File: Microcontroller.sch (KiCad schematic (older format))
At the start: 14 parts, among them SW1 SW_Push, SW2 SW_Push, U2 PIC16F1939-IPT, Y1 Crystal

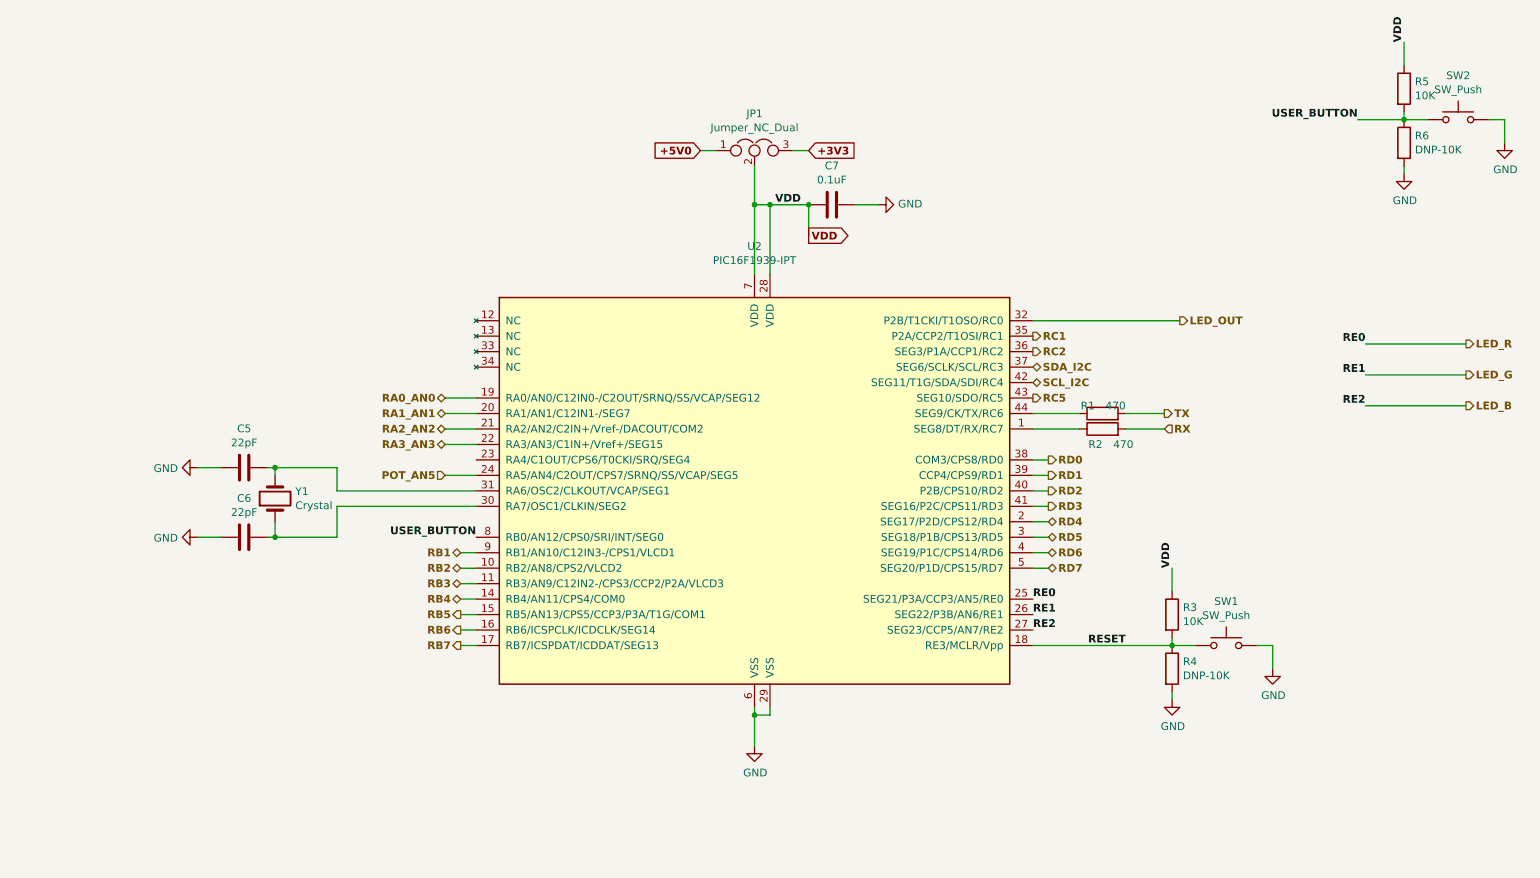
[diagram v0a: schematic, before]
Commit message: Se agrega bus a jerarquia y pines de programación icsp
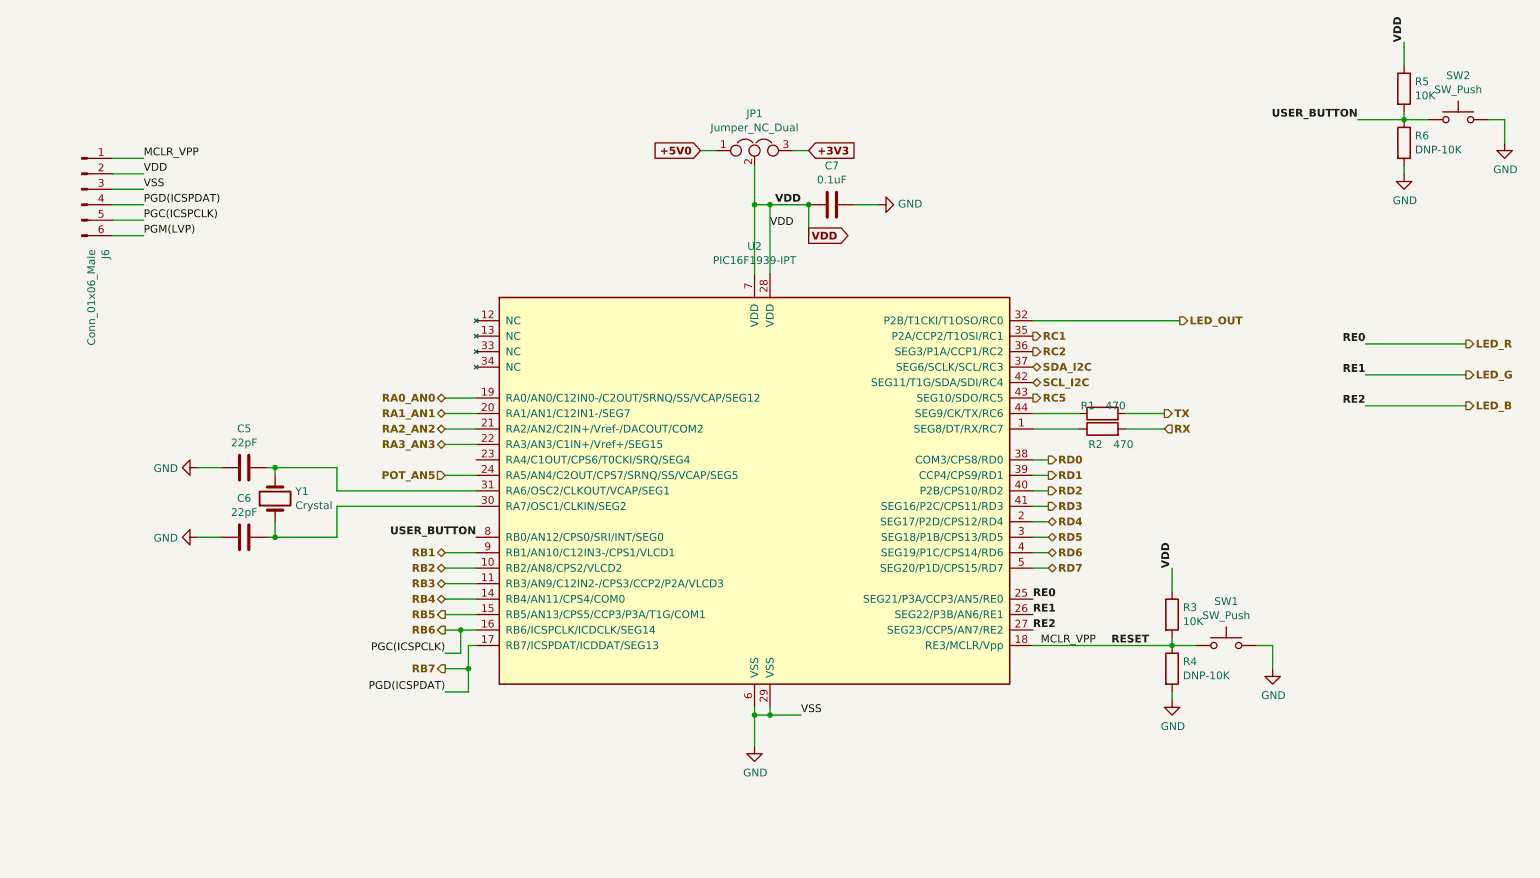
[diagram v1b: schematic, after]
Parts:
- added J6: Conn_01x06_Male, symbol Connector:Conn_01x06_Male
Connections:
- net GND: now also J6.3 (Pin_3)
- net RB6: now also J6.5 (Pin_5)
- net RB7: now also J6.4 (Pin_4)
- net VDD: now also J6.2 (Pin_2)
- net RESET renamed MCLR_VPP
- net MCLR_VPP: now also J6.1 (Pin_1)
- new net PGM(LVP): J6.6 (Pin_6)
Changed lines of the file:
@@
 EESchema Schematic File Version 4
+LIBS:TPDSI_1-cache
 EELAYER 29 0
 EELAYER END
@@
 Sheet 2 5
 Title "Kit Development for MCU PIC"
-Date "2019-05-05"
-Rev "1.0"
+Date "2019-05-06"
+Rev "1.1"
 Comp "Julian Bustamante Narvaez"
 Comment1 ""
@@
 	1    0    0    -1
 $EndComp
-Wire Wire Line
-	5850 5250 5850 5300
-Wire Wire Line
-	5950 5300 5950 5250
-Wire Wire Line
-	5850 5300 5950 5300
-Wire Wire Line
-	5850 5500 5850 5300
-Connection ~ 5850 5300
 $Comp
 L power:GND #PWR010
@@
 Text Label 4050 4150 2    50   ~ 10
 USER_BUTTON
-Text Label 8250 4850 2    50   ~ 10
+Text Label 8400 4850 2    50   ~ 10
 RESET
 Wire Wire Line
@@
 	1    0    0    -1
 $EndComp
-Wire Wire Line
-	4050 4850 3950 4850
-Text HLabel 3950 4850 0    50   Output ~ 10
+Text HLabel 3850 5000 0    50   Output ~ 10
 RB7
-Wire Wire Line
-	4050 4750 3950 4750
-Text HLabel 3950 4750 0    50   Output ~ 10
+Text HLabel 3850 4750 0    50   Output ~ 10
 RB6
-Wire Wire Line
-	4050 4650 3950 4650
-Text HLabel 3950 4650 0    50   Output ~ 10
+Text HLabel 3850 4650 0    50   Output ~ 10
 RB5
-Wire Wire Line
-	4050 4550 3950 4550
-Text HLabel 3950 4550 0    50   BiDi ~ 10
+Text HLabel 3850 4550 0    50   BiDi ~ 10
 RB4
-Wire Wire Line
-	4050 4450 3950 4450
-Text HLabel 3950 4450 0    50   BiDi ~ 10
+Text HLabel 3850 4450 0    50   BiDi ~ 10
 RB3
-Wire Wire Line
-	4050 4350 3950 4350
-Text HLabel 3950 4350 0    50   BiDi ~ 10
+Text HLabel 3850 4350 0    50   BiDi ~ 10
 RB2
-Wire Wire Line
-	4050 4250 3950 4250
-Text HLabel 3950 4250 0    50   BiDi ~ 10
+Text HLabel 3850 4250 0    50   BiDi ~ 10
 RB1
 Text HLabel 7650 2850 2    50   Output ~ 10
@@
 	6200 2200 6200 2000
 Connection ~ 6200 2000
+$Comp
+L Connector:Conn_01x06_Male J6
+U 1 1 5CD0F49A
+P 1500 1900
+F 0 "J6" V 1654 1512 50  0000 R CNN
+F 1 "Conn_01x06_Male" V 1563 1512 50  0000 R CNN
+F 2 "" H 1500 1900 50  0001 C CNN
+F 3 "~" H 1500 1900 50  0001 C CNN
+	1    1500 1900
+	1    0    0    -1
+$EndComp
+Wire Wire Line
+	1700 1700 1900 1700
+Wire Wire Line
+	1700 1800 1900 1800
+Wire Wire Line
+	1700 1900 1900 1900
+Wire Wire Line
+	1700 2000 1900 2000
+Wire Wire Line
+	1900 2100 1700 2100
+Wire Wire Line
+	1700 2200 1900 2200
+Text Label 1900 2200 0    50   ~ 0
+PGM(LVP)
+Text Label 1900 2100 0    50   ~ 0
+PGC(ICSPCLK)
+Text Label 1900 2000 0    50   ~ 0
+PGD(ICSPDAT)
+Text Label 1900 1900 0    50   ~ 0
+VSS
+Text Label 1900 1800 0    50   ~ 0
+VDD
+Text Label 1900 1700 0    50   ~ 0
+MCLR_VPP
+Text Label 3850 5150 2    50   ~ 0
+PGD(ICSPDAT)
+Text Label 7700 4850 0    50   ~ 0
+MCLR_VPP
+Text Label 5950 2150 0    50   ~ 0
+VDD
+Text Label 6150 5300 0    50   ~ 0
+VSS
+Wire Wire Line
+	5850 5250 5850 5300
+Wire Wire Line
+	6150 5300 5950 5300
+Wire Wire Line
+	5950 5300 5950 5250
+Wire Wire Line
+	5950 5300 5850 5300
+Connection ~ 5950 5300
+Connection ~ 5850 5300
+Wire Wire Line
+	5850 5300 5850 5500
+Text Label 3850 4900 2    50   ~ 0
+PGC(ICSPCLK)
+Wire Wire Line
+	4000 4850 4000 5000
+Wire Wire Line
+	3850 5000 4000 5000
+Connection ~ 4000 5000
+Wire Wire Line
+	3850 5150 4000 5150
+Wire Wire Line
+	4000 5000 4000 5150
+Wire Wire Line
+	3850 4750 3950 4750
+Wire Wire Line
+	4000 4850 4050 4850
+Connection ~ 3950 4750
+Wire Wire Line
+	3950 4750 4050 4750
+Wire Wire Line
+	3850 4250 4050 4250
+Wire Wire Line
+	3850 4350 4050 4350
+Wire Wire Line
+	3850 4450 4050 4450
+Wire Wire Line
+	3850 4550 4050 4550
+Wire Wire Line
+	3850 4650 4050 4650
+Wire Wire Line
+	3950 4900 3850 4900
+Wire Wire Line
+	3950 4750 3950 4900
 $EndSCHEMATC

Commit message: Se Organiza conexiones de alimentacion con elementos de la biblioteca power, se quitan algunas etiquetas y se coloca la fuente en hoja principal
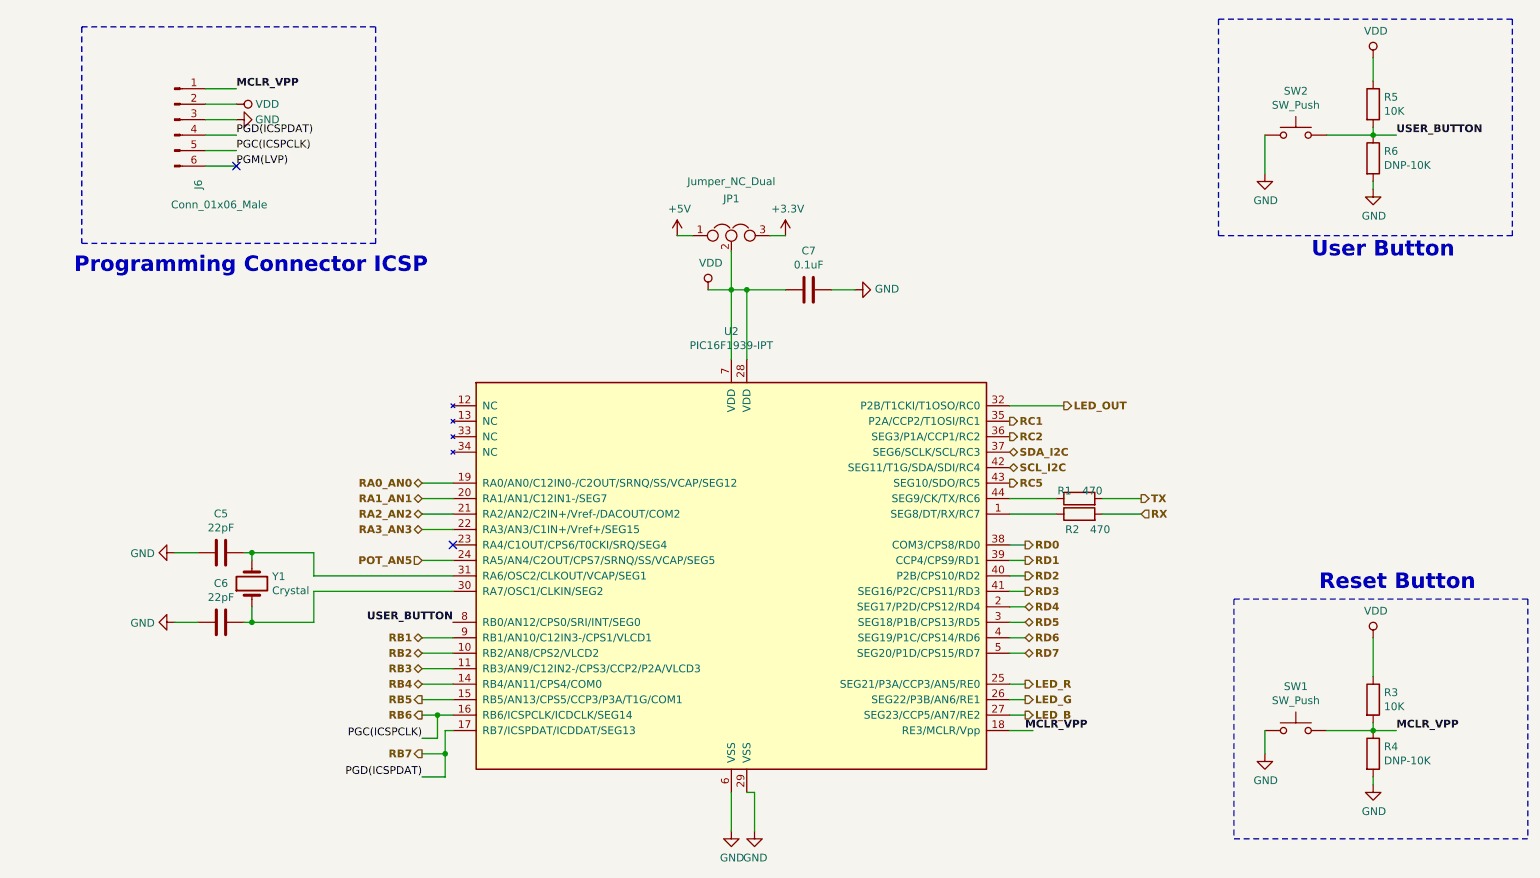
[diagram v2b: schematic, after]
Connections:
- net GND: now also SW1.1, SW2.1; no longer SW1.2, SW2.2
- net MCLR_VPP: now also SW1.2; no longer SW1.1
- net USER_BUTTON: now also SW2.2; no longer SW2.1
- net +5V0 renamed +5V
- no-connect marks 0 -> 2
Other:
- note added: "Programming Connector ICSP"
- note added: "Reset Button"
- note added: "User Button"
- moved on the sheet: C5, C6, C7, J6, JP1, R1, R2, R3, R4, R5, R6, SW1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

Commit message: Se agregan recomendaciones izq->dcha (In/Out), se Reorganiza jerarquía y bus de datos, se coloca graphics lines para indicar submodulos
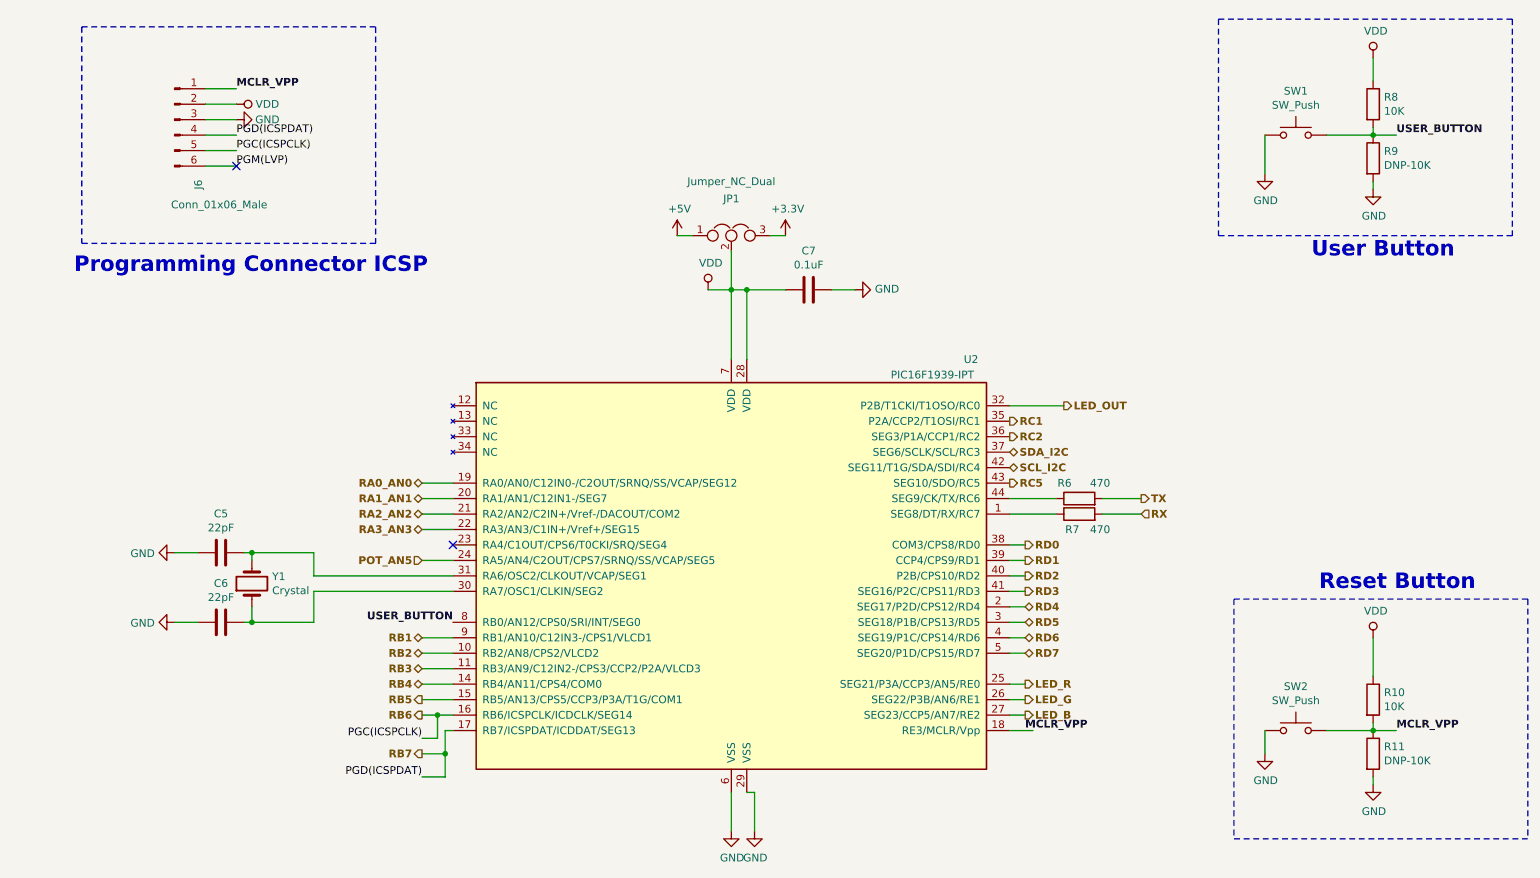
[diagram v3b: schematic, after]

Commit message: Se agrega ubicación de componentes, asociación de footprint, pendiente Ruteo.
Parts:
- C5, C6: footprint (none) -> Capacitor_SMD:C_0603_1608Metric; Part Number (none) -> 732-7748-1-ND
- C7: footprint (none) -> Capacitor_SMD:C_0603_1608Metric; Part Number (none) -> 732-7939-1-ND
- J6: footprint (none) -> Connector_PinSocket_2.54mm:PinSocket_1x06_P2.54mm_Vertical
- JP1: footprint (none) -> Connector_PinSocket_2.54mm:PinSocket_1x03_P2.54mm_Vertical
- R1, R2, R3, R4, R5, R6: footprint (none) -> Resistor_SMD:R_0603_1608Metric_Pad1.05x0.95mm_HandSolder
- SW1, SW2: footprint (none) -> Button_Switch_THT:SW_PUSH_6mm_H5mm; Part Number (none) -> 450-1804-ND
- U2: footprint (none) -> Package_QFP:TQFP-44_10x10mm_P0.8mm
- Y1: footprint (none) -> Crystal:Crystal_HC18-U_Vertical
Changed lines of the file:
@@
 F 0 "JP1" H 5700 2439 50  0000 C CNN
 F 1 "Jumper_NC_Dual" H 5700 2550 50  0000 C CNN
-F 2 "" H 5700 2200 50  0001 C CNN
+F 2 "Connector_PinSocket_2.54mm:PinSocket_1x03_P2.54mm_Vertical" H 5700 2200 50  0001 C CNN
 F 3 "~" H 5700 2200 50  0001 C CNN
 	1    5700 2200
@@
 F 0 "Y1" V 2646 4319 50  0000 R CNN
 F 1 "Crystal" V 2555 4319 50  0000 R CNN
-F 2 "" H 2600 4450 50  0001 C CNN
+F 2 "Crystal:Crystal_HC18-U_Vertical" H 2600 4450 50  0001 C CNN
 F 3 "~" H 2600 4450 50  0001 C CNN
 	1    2600 4450
@@
 F 0 "C5" V 2652 4250 50  0000 C CNN
 F 1 "22pF" V 2561 4250 50  0000 C CNN
-F 2 "" H 2438 4100 50  0001 C CNN
+F 2 "Capacitor_SMD:C_0603_1608Metric" H 2438 4100 50  0001 C CNN
 F 3 "~" H 2400 4250 50  0001 C CNN
+F 4 "732-7748-1-ND" V 2400 4250 50  0001 C CNN "Part Number"
 	1    2400 4250
 	0    -1   -1   0
@@
 F 0 "C6" V 2652 4700 50  0000 C CNN
 F 1 "22pF" V 2561 4700 50  0000 C CNN
-F 2 "" H 2438 4550 50  0001 C CNN
+F 2 "Capacitor_SMD:C_0603_1608Metric" H 2438 4550 50  0001 C CNN
 F 3 "~" H 2400 4700 50  0001 C CNN
+F 4 "732-7748-1-ND" V 2400 4700 50  0001 C CNN "Part Number"
 	1    2400 4700
 	0    -1   -1   0
@@
 F 0 "SW2" H 9350 5685 50  0000 C CNN
 F 1 "SW_Push" H 9350 5594 50  0000 C CNN
-F 2 "" H 9350 5600 50  0001 C CNN
+F 2 "Button_Switch_THT:SW_PUSH_6mm_H5mm" H 9350 5600 50  0001 C CNN
 F 3 "~" H 9350 5600 50  0001 C CNN
+F 4 "450-1804-ND" H 9350 5400 50  0001 C CNN "Part Number"
 	1    9350 5400
 	1    0    0    -1
@@
 F 0 "R10" H 9920 5246 50  0000 L CNN
 F 1 "10K" H 9920 5155 50  0000 L CNN
-F 2 "" V 9780 5200 50  0001 C CNN
+F 2 "Resistor_SMD:R_0603_1608Metric_Pad1.05x0.95mm_HandSolder" V 9780 5200 50  0001 C CNN
 F 3 "~" H 9850 5200 50  0001 C CNN
 	1    9850 5200
@@
 F 0 "C7" V 5948 2550 50  0000 C CNN
 F 1 "0.1uF" V 6039 2550 50  0000 C CNN
-F 2 "" H 6238 2400 50  0001 C CNN
+F 2 "Capacitor_SMD:C_0603_1608Metric" H 6238 2400 50  0001 C CNN
 F 3 "~" H 6200 2550 50  0001 C CNN
+F 4 "732-7939-1-ND" V 6200 2550 50  0001 C CNN "Part Number"
 	1    6200 2550
 	0    1    1    0
@@
 F 0 "R11" H 9920 5596 50  0000 L CNN
 F 1 "DNP-10K" H 9920 5505 50  0000 L CNN
-F 2 "" V 9780 5550 50  0001 C CNN
+F 2 "Resistor_SMD:R_0603_1608Metric_Pad1.05x0.95mm_HandSolder" V 9780 5550 50  0001 C CNN
 F 3 "~" H 9850 5550 50  0001 C CNN
 	1    9850 5550
@@
 F 0 "SW1" H 9350 1835 50  0000 C CNN
 F 1 "SW_Push" H 9350 1744 50  0000 C CNN
-F 2 "" H 9350 1750 50  0001 C CNN
+F 2 "Button_Switch_THT:SW_PUSH_6mm_H5mm" H 9350 1750 50  0001 C CNN
 F 3 "~" H 9350 1750 50  0001 C CNN
+F 4 "450-1804-ND" H 9350 1550 50  0001 C CNN "Part Number"
 	1    9350 1550
 	1    0    0    -1
@@
 F 0 "R8" H 9920 1396 50  0000 L CNN
 F 1 "10K" H 9920 1305 50  0000 L CNN
-F 2 "" V 9780 1350 50  0001 C CNN
+F 2 "Resistor_SMD:R_0603_1608Metric_Pad1.05x0.95mm_HandSolder" V 9780 1350 50  0001 C CNN
 F 3 "~" H 9850 1350 50  0001 C CNN
 	1    9850 1350
@@
 F 0 "R9" H 9920 1746 50  0000 L CNN
 F 1 "DNP-10K" H 9920 1655 50  0000 L CNN
-F 2 "" V 9780 1700 50  0001 C CNN
+F 2 "Resistor_SMD:R_0603_1608Metric_Pad1.05x0.95mm_HandSolder" V 9780 1700 50  0001 C CNN
 F 3 "~" H 9850 1700 50  0001 C CNN
 	1    9850 1700
@@
 F 0 "R6" V 8050 3950 50  0000 L CNN
 F 1 "470" V 8050 3700 50  0000 L CNN
-F 2 "" V 7880 3900 50  0001 C CNN
+F 2 "Resistor_SMD:R_0603_1608Metric_Pad1.05x0.95mm_HandSolder" V 7880 3900 50  0001 C CNN
 F 3 "~" H 7950 3900 50  0001 C CNN
 	1    7950 3900
@@
 F 0 "R7" V 7850 4000 50  0000 L CNN
 F 1 "470" V 7850 3800 50  0000 L CNN
-F 2 "" V 7880 4000 50  0001 C CNN
+F 2 "Resistor_SMD:R_0603_1608Metric_Pad1.05x0.95mm_HandSolder" V 7880 4000 50  0001 C CNN
 F 3 "~" H 7950 4000 50  0001 C CNN
 	1    7950 4000
@@
 F 0 "U2" H 7250 5800 50  0000 C CNN
 F 1 "PIC16F1939-IPT" H 7000 5700 50  0000 C CNN
-F 2 "" H 5700 4400 50  0001 C CNN
+F 2 "Package_QFP:TQFP-44_10x10mm_P0.8mm" H 5700 4400 50  0001 C CNN
 F 3 "http://ww1.microchip.com/downloads/en/DeviceDoc/41364E.pdf" H 5700 4400 50  0001 C CNN
 	1    5700 4400
@@
 F 0 "J6" V 2254 1062 50  0000 R CNN
 F 1 "Conn_01x06_Male" H 2700 900 50  0000 R CNN
-F 2 "" H 2100 1450 50  0001 C CNN
+F 2 "Connector_PinSocket_2.54mm:PinSocket_1x06_P2.54mm_Vertical" H 2100 1450 50  0001 C CNN
 F 3 "~" H 2100 1450 50  0001 C CNN
 	1    2100 1450
